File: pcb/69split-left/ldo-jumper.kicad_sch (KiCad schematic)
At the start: 4 parts, among them U2 TLV76133DCY

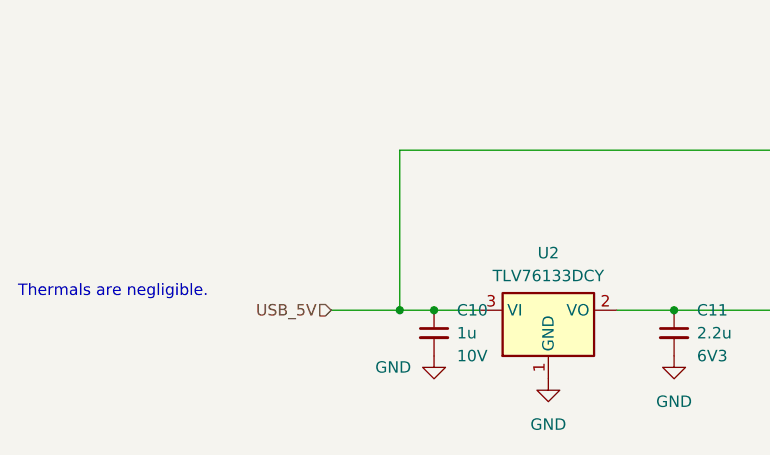
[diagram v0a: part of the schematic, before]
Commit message: Started changing things gain to use an I/O expander with I2C.
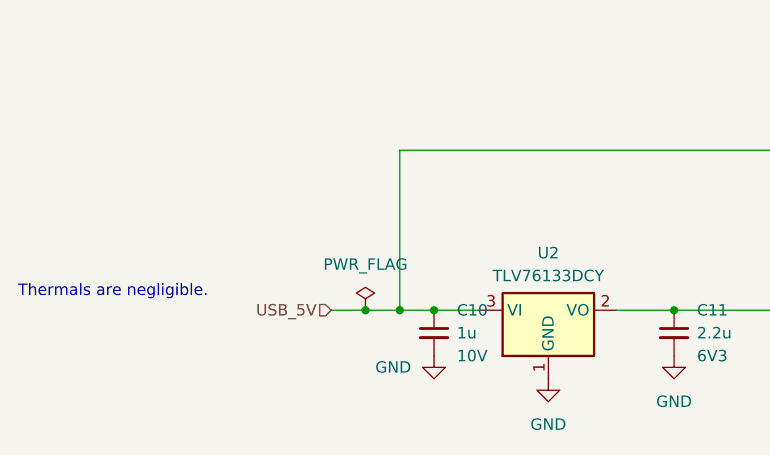
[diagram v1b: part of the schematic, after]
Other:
- company: (none) -> Yiannis Michael
- title: 69SPLIT KEYBOARD -> 69SPLIT
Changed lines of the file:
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@@
 	(paper "A5")
 	(title_block
-		(title "69SPLIT KEYBOARD")
-		(date "2025-06-21")
+		(title "69SPLIT")
+		(date "2025-07-28")
 		(rev "1")
+		(company "Yiannis Michael")
 		(comment 1 "Yiannis Michael")
 		(comment 2 "ymich9963")
@@
 		(color 0 0 0 0)
 	)
+	(junction
+		(at 76.2 76.2)
+		(diameter 0)
+		(color 0 0 0 0)
+	)
 	(wire
 		(pts
@@
 	(wire
 		(pts
-			(xy 72.39 76.2) (xy 80.01 76.2)
+			(xy 76.2 76.2) (xy 80.01 76.2)
+		)
+		(stroke
+			(width 0)
+			(type default)
+		)
+	)
+	(wire
+		(pts
+			(xy 72.39 76.2) (xy 76.2 76.2)
 		)
 		(stroke
@@
 		)
 		(instances
+			(project "69split"
+				(path "/1573ac28-80e2-4ab2-b20c-1c4896f37ece/800133d0-6e68-49ca-a870-e06397f7c02c/cd421ade-5253-45fb-9a51-28ad04a50b20"
+					(reference "U?")
+					(unit 1)
+				)
+			)
 			(project "69split-left"
 				(path "/94301c1c-44b1-4926-ac38-8a25b84a2b23/cd421ade-5253-45fb-9a51-28ad04a50b20"
@@
 		(dnp no)
 		(fields_autoplaced yes)
-		(property "Reference" "#PWR024"
+		(property "Reference" "#PWR021"
 			(at 83.82 87.63 0)
 			(effects
@@
 		)
 		(instances
+			(project "69split"
+				(path "/1573ac28-80e2-4ab2-b20c-1c4896f37ece/800133d0-6e68-49ca-a870-e06397f7c02c/cd421ade-5253-45fb-9a51-28ad04a50b20"
+					(reference "#PWR?")
+					(unit 1)
+				)
+			)
 			(project "69split-left"
 				(path "/94301c1c-44b1-4926-ac38-8a25b84a2b23/cd421ade-5253-45fb-9a51-28ad04a50b20"
-					(reference "#PWR024")
+					(reference "#PWR021")
 					(unit 1)
 				)
@@
 		(dnp no)
 		(fields_autoplaced yes)
-		(property "Reference" "#PWR025"
+		(property "Reference" "#PWR022"
 			(at 110.49 87.63 0)
 			(effects
@@
 		)
 		(instances
+			(project "69split"
+				(path "/1573ac28-80e2-4ab2-b20c-1c4896f37ece/800133d0-6e68-49ca-a870-e06397f7c02c/cd421ade-5253-45fb-9a51-28ad04a50b20"
+					(reference "#PWR?")
+					(unit 1)
+				)
+			)
 			(project "69split-left"
 				(path "/94301c1c-44b1-4926-ac38-8a25b84a2b23/cd421ade-5253-45fb-9a51-28ad04a50b20"
-					(reference "#PWR025")
+					(reference "#PWR022")
 					(unit 1)
 				)
@@
 		(dnp no)
 		(fields_autoplaced yes)
-		(property "Reference" "#PWR026"
+		(property "Reference" "#PWR023"
 			(at 96.52 90.17 0)
 			(effects
@@
 		)
 		(instances
+			(project "69split"
+				(path "/1573ac28-80e2-4ab2-b20c-1c4896f37ece/800133d0-6e68-49ca-a870-e06397f7c02c/cd421ade-5253-45fb-9a51-28ad04a50b20"
+					(reference "#PWR?")
+					(unit 1)
+				)
+			)
 			(project "69split-left"
 				(path "/94301c1c-44b1-4926-ac38-8a25b84a2b23/cd421ade-5253-45fb-9a51-28ad04a50b20"
-					(reference "#PWR026")
+					(reference "#PWR023")
 					(unit 1)
 				)
@@
 		)
 		(instances
+			(project "69split"
+				(path "/1573ac28-80e2-4ab2-b20c-1c4896f37ece/800133d0-6e68-49ca-a870-e06397f7c02c/cd421ade-5253-45fb-9a51-28ad04a50b20"
+					(reference "C?")
+					(unit 1)
+				)
+			)
 			(project "69split-left"
 				(path "/94301c1c-44b1-4926-ac38-8a25b84a2b23/cd421ade-5253-45fb-9a51-28ad04a50b20"
@@
 		)
 		(instances
+			(project "69split"
+				(path "/1573ac28-80e2-4ab2-b20c-1c4896f37ece/800133d0-6e68-49ca-a870-e06397f7c02c/cd421ade-5253-45fb-9a51-28ad04a50b20"
+					(reference "JP?")
+					(unit 1)
+				)
+			)
 			(project "69split-left"
 				(path "/94301c1c-44b1-4926-ac38-8a25b84a2b23/cd421ade-5253-45fb-9a51-28ad04a50b20"
 					(reference "JP1")
+					(unit 1)
+				)
+			)
+		)
+	)
+	(symbol
+		(lib_id "power:PWR_FLAG")
+		(at 76.2 76.2 0)
+		(unit 1)
+		(exclude_from_sim no)
+		(in_bom yes)
+		(on_board yes)
+		(dnp no)
+		(fields_autoplaced yes)
+		(property "Reference" "#FLG03"
+			(at 76.2 74.295 0)
+			(effects
+				(font
+					(size 1.27 1.27)
+				)
+				(hide yes)
+			)
+		)
+		(property "Value" "PWR_FLAG"
+			(at 76.2 71.12 0)
+			(effects
+				(font
+					(size 1.27 1.27)
+				)
+			)
+		)
+		(property "Footprint" ""
+			(at 76.2 76.2 0)
+			(effects
+				(font
+					(size 1.27 1.27)
+				)
+				(hide yes)
+			)
+		)
+		(property "Datasheet" "~"
+			(at 76.2 76.2 0)
+			(effects
+				(font
+					(size 1.27 1.27)
+				)
+				(hide yes)
+			)
+		)
+		(property "Description" "Special symbol for telling ERC where power comes from"
+			(at 76.2 76.2 0)
+			(effects
+				(font
+					(size 1.27 1.27)
+				)
+				(hide yes)
+			)
+		)
+		(pin "1"
+		)
+		(instances
+			(project "69split-left"
+				(path "/94301c1c-44b1-4926-ac38-8a25b84a2b23/cd421ade-5253-45fb-9a51-28ad04a50b20"
+					(reference "#FLG03")
 					(unit 1)
 				)
@@
 		)
 		(instances
+			(project "69split"
+				(path "/1573ac28-80e2-4ab2-b20c-1c4896f37ece/800133d0-6e68-49ca-a870-e06397f7c02c/cd421ade-5253-45fb-9a51-28ad04a50b20"
+					(reference "C?")
+					(unit 1)
+				)
+			)
 			(project "69split-left"
 				(path "/94301c1c-44b1-4926-ac38-8a25b84a2b23/cd421ade-5253-45fb-9a51-28ad04a50b20"

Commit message: Finished left keyboard again...
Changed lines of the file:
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@@
+		(color 0 0 0 0)
+	)
+	(junction
+		(at 134.62 76.2)
+		(diameter 0)
 		(color 0 0 0 0)
 	)
@@
 		(pts
 			(xy 104.14 76.2) (xy 110.49 76.2)
+		)
+		(stroke
+			(width 0)
+			(type default)
+		)
+	)
+	(wire
+		(pts
+			(xy 134.62 85.09) (xy 158.75 85.09)
 		)
 		(stroke
@@
 	(wire
 		(pts
+			(xy 134.62 76.2) (xy 134.62 85.09)
+		)
+		(stroke
+			(width 0)
+			(type default)
+		)
+	)
+	(wire
+		(pts
 			(xy 134.62 58.42) (xy 134.62 60.96)
 		)
@@
 		)
 	)
-	(label "3V3"
-		(at 123.19 76.2 0)
+	(hierarchical_label "3V3"
+		(shape input)
+		(at 158.75 85.09 0)
 		(effects
 			(font
 				(size 1.27 1.27)
 			)
-			(justify left bottom)
+			(justify left)
 		)
 	)

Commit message: Added ESD protection and better routing for the USB data lines.
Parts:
- JP1: MPN (none) -> Generic
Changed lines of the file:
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@@
+			)
+		)
+		(property "MPN" "Generic"
+			(at 134.62 67.31 90)
+			(effects
+				(font
+					(size 1.27 1.27)
+				)
+				(hide yes)
 			)
 		)
